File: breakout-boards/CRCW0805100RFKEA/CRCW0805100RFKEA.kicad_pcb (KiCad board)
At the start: 2 copper layers, 14 parts, among them J1 Conn_01x12, J2 Conn_01x12

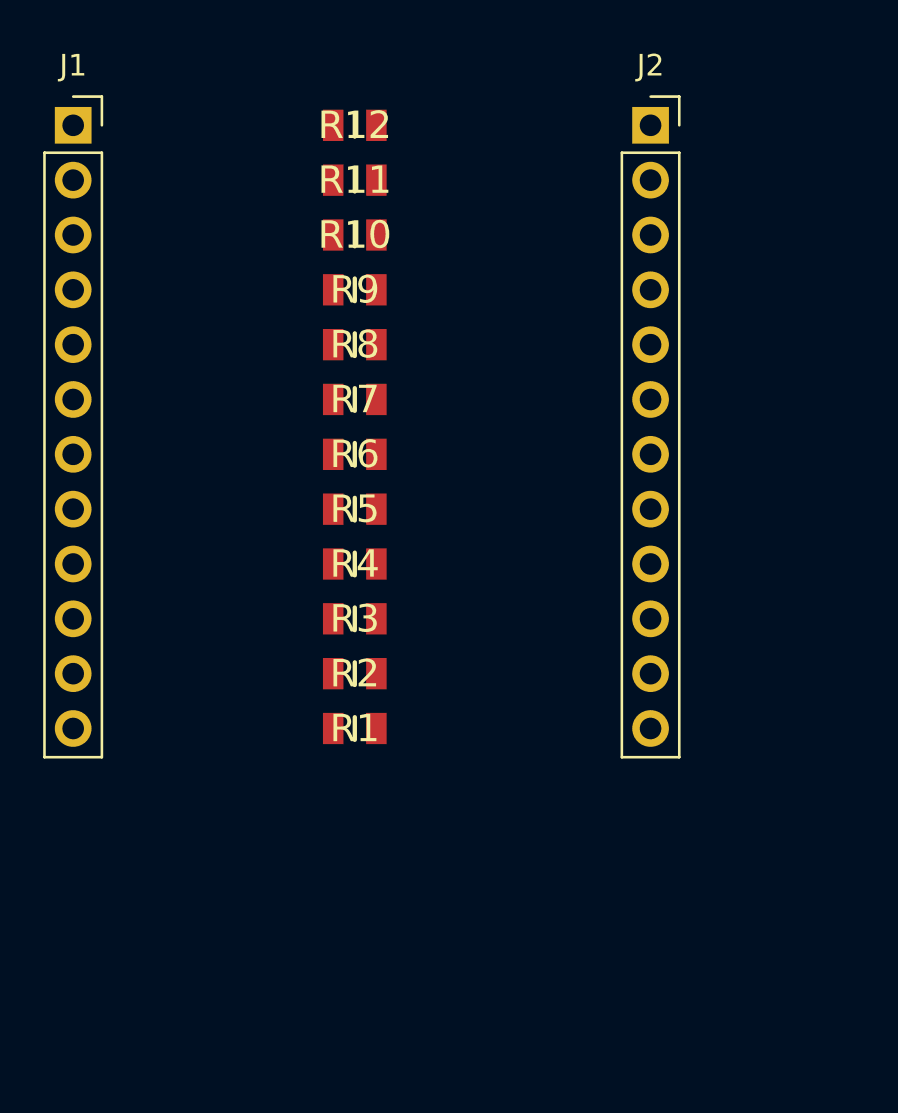
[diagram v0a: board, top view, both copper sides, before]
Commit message: feat: create footprints for resistor breakout boards
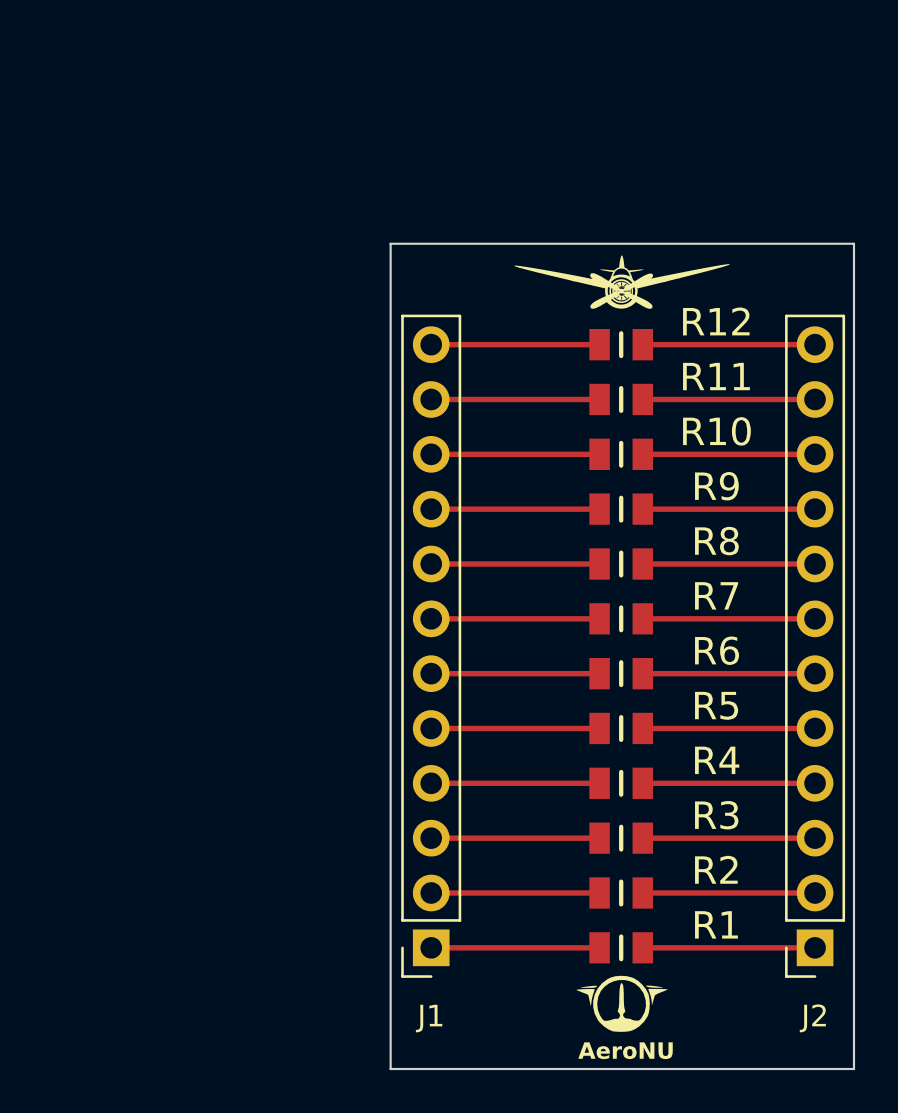
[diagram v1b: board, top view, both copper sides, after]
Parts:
- added AeroNU: LOGO, FixedWing:AeroNU - Logo (Smol), F.Cu at (161.4, 109.5)
- added FixedWing: LOGO, FixedWing:FixedWing - Logo (Smol), F.Cu at (161.3, 74.0)
- moved J1 41.6 mm to (152.4, 104.1), turned to 180 degrees
- moved J2 38.9 mm to (170.2, 104.1), turned to 180 degrees
- moved R5 16.0 mm to (161.2, 94.0)
- moved R7 16.0 mm to (161.2, 88.9)
- moved R1 16.0 mm to (161.2, 104.1)
- moved R10 16.0 mm to (161.2, 81.3)
- moved R11 16.0 mm to (161.2, 78.7)
- moved R12 16.0 mm to (161.2, 76.2)
- moved R2 16.0 mm to (161.2, 101.6)
- moved R3 16.0 mm to (161.2, 99.1)
- moved R4 16.0 mm to (161.2, 96.5)
- moved R6 16.0 mm to (161.2, 91.4)
- moved R8 16.0 mm to (161.2, 86.4)
- moved R9 16.0 mm to (161.2, 83.8)
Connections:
- R1 pad 1: Net-(J1-Pin_12) -> Net-(J1-Pin_1)
- R1 pad 2: Net-(J2-Pin_12) -> Net-(J2-Pin_1)
- R10 pad 1: Net-(J1-Pin_3) -> Net-(J1-Pin_10)
- R10 pad 2: Net-(J2-Pin_3) -> Net-(J2-Pin_10)
- R11 pad 1: Net-(J1-Pin_2) -> Net-(J1-Pin_11)
- R11 pad 2: Net-(J2-Pin_2) -> Net-(J2-Pin_11)
- R12 pad 1: Net-(J1-Pin_1) -> Net-(J1-Pin_12)
- R12 pad 2: Net-(J2-Pin_1) -> Net-(J2-Pin_12)
- R2 pad 1: Net-(J1-Pin_11) -> Net-(J1-Pin_2)
- R2 pad 2: Net-(J2-Pin_11) -> Net-(J2-Pin_2)
- R3 pad 1: Net-(J1-Pin_10) -> Net-(J1-Pin_3)
- R3 pad 2: Net-(J2-Pin_10) -> Net-(J2-Pin_3)
- R4 pad 1: Net-(J1-Pin_9) -> Net-(J1-Pin_4)
- R4 pad 2: Net-(J2-Pin_9) -> Net-(J2-Pin_4)
- R5 pad 1: Net-(J1-Pin_8) -> Net-(J1-Pin_5)
- R5 pad 2: Net-(J2-Pin_8) -> Net-(J2-Pin_5)
- R6 pad 1: Net-(J1-Pin_7) -> Net-(J1-Pin_6)
- R6 pad 2: Net-(J2-Pin_7) -> Net-(J2-Pin_6)
- R7 pad 1: Net-(J1-Pin_6) -> Net-(J1-Pin_7)
- R7 pad 2: Net-(J2-Pin_6) -> Net-(J2-Pin_7)
- R8 pad 1: Net-(J1-Pin_5) -> Net-(J1-Pin_8)
- R8 pad 2: Net-(J2-Pin_5) -> Net-(J2-Pin_8)
- R9 pad 1: Net-(J1-Pin_4) -> Net-(J1-Pin_9)
- R9 pad 2: Net-(J2-Pin_4) -> Net-(J2-Pin_9)
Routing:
- net Net-(J2-Pin_9): track 0.00 -> 7.98 mm
- net Net-(J2-Pin_8): track 0.00 -> 7.98 mm
- net Net-(J2-Pin_7): track 0.00 -> 7.98 mm
- net Net-(J2-Pin_6): track 0.00 -> 7.98 mm
- net Net-(J2-Pin_5): track 0.00 -> 7.98 mm
- net Net-(J2-Pin_4): track 0.00 -> 7.98 mm
- net Net-(J2-Pin_3): track 0.00 -> 7.98 mm
- net Net-(J2-Pin_2): track 0.00 -> 7.98 mm
- net Net-(J2-Pin_12): track 0.00 -> 7.98 mm
- net Net-(J2-Pin_11): track 0.00 -> 7.98 mm
- net Net-(J2-Pin_10): track 0.00 -> 7.98 mm
- net Net-(J2-Pin_1): track 0.00 -> 7.98 mm
- net Net-(J1-Pin_9): track 0.00 -> 7.80 mm
- net Net-(J1-Pin_8): track 0.00 -> 7.80 mm
- net Net-(J1-Pin_7): track 0.00 -> 7.80 mm
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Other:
- board outline added: 21.5 x 38.2 mm
- board text added: "AeroNU"
- board text added: "Designed By Ephram CJ and Matthew F"

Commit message: feat: finalize 100ohm board design
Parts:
- moved R1 4.17 mm to (165.4, 104.1)
- moved R10 4.17 mm to (165.4, 81.3)
- moved R4 4.17 mm to (165.4, 96.5)
- moved R7 4.17 mm to (165.4, 88.9)
- moved FixedWing 4.14 mm to (165.3, 73.2)
- moved AeroNU 4.05 mm to (157.3, 109.4)
- moved R12 3.99 mm to (157.2, 76.2)
- moved R3 3.99 mm to (157.2, 99.1)
- moved R6 3.99 mm to (157.2, 91.4)
- moved R9 3.99 mm to (157.2, 83.8)
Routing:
- net Net-(J2-Pin_7): track 7.98 -> 3.81 mm
- net Net-(J2-Pin_4): track 7.98 -> 3.81 mm
- net Net-(J2-Pin_10): track 7.98 -> 3.81 mm
- net Net-(J2-Pin_1): track 7.98 -> 3.81 mm
- net Net-(J1-Pin_7): track 7.80 -> 12.0 mm
- net Net-(J1-Pin_4): track 7.80 -> 12.0 mm
- net Net-(J1-Pin_10): track 7.80 -> 12.0 mm
- net Net-(J1-Pin_1): track 7.80 -> 12.0 mm
- net Net-(J2-Pin_9): track 7.98 -> 12.0 mm
- net Net-(J2-Pin_6): track 7.98 -> 12.0 mm
- net Net-(J2-Pin_3): track 7.98 -> 12.0 mm
- net Net-(J2-Pin_12): track 7.98 -> 12.0 mm
- net Net-(J1-Pin_9): track 7.80 -> 3.81 mm
- net Net-(J1-Pin_6): track 7.80 -> 3.81 mm
- net Net-(J1-Pin_3): track 7.80 -> 3.81 mm
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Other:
- board size 21.5 x 38.2 mm -> 21.5 x 38.7 mm
